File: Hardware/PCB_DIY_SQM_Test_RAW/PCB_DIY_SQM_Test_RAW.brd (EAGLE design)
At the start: 53 x 59.7 mm, 10 parts, among them U1 MLX90614_, U2 ARDUINO_SHIELDLONGPADS

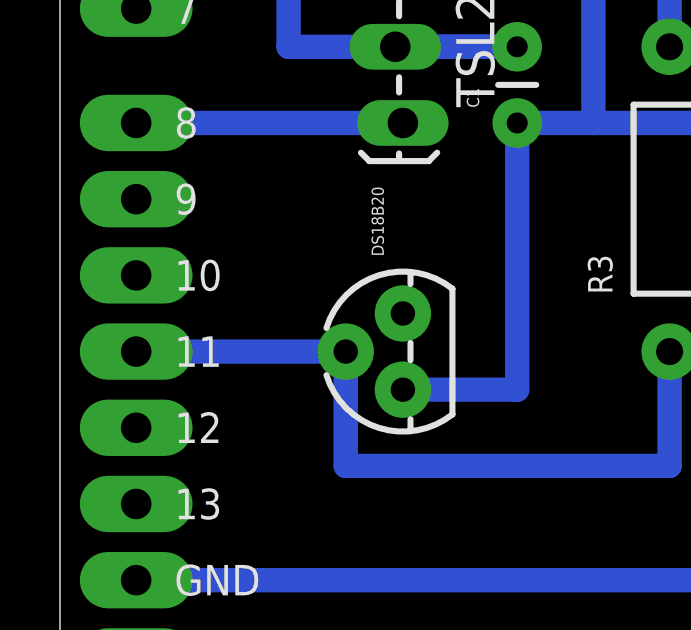
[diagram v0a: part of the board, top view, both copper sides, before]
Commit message: The DS18B20 now connects to Arduino pin #10 instead of pin #11. This allows us to use the Wireless SD shield (which uses pin #11 for SPI)
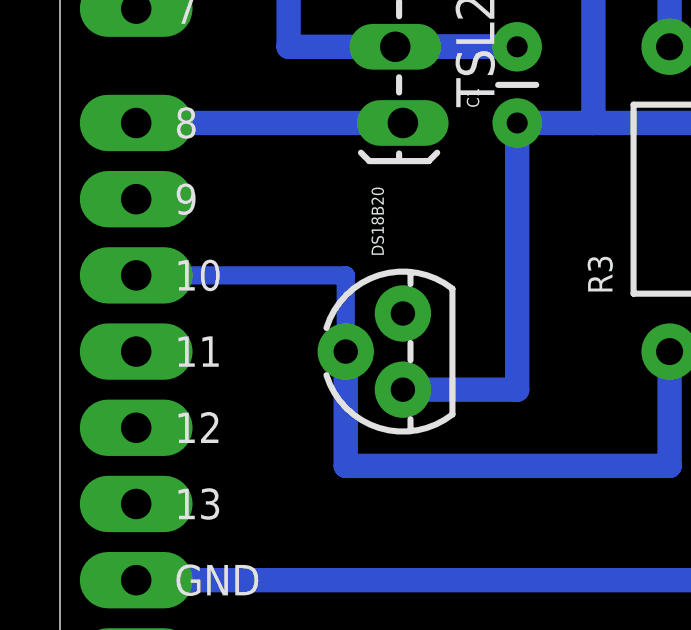
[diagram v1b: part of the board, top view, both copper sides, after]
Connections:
- net DS18B20P2: now also U2.D10; no longer U2.D11
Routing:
- net DS18B20P2: track 25.4 -> 27.9 mm
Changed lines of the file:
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@@
 <signal name="DS18B20P2">
 <contactref element="DS18B20" pad="2"/>
-<contactref element="U2" pad="D11"/>
 <contactref element="R3" pad="P$1"/>
 <wire x1="20.32" y1="25.4" x2="20.32" y2="21.59" width="0.8128" layer="16"/>
 <wire x1="20.32" y1="21.59" x2="9.525" y2="21.59" width="0.8128" layer="16"/>
 <wire x1="9.525" y1="21.59" x2="9.525" y2="25.4" width="0.8128" layer="16"/>
-<wire x1="9.525" y1="25.4" x2="2.54" y2="25.4" width="0.8128" layer="16"/>
+<contactref element="U2" pad="D10"/>
+<wire x1="2.54" y1="27.94" x2="9.525" y2="27.94" width="0.6096" layer="16"/>
+<wire x1="9.525" y1="27.94" x2="9.525" y2="25.4" width="0.6096" layer="16"/>
 </signal>
 <signal name="5V">

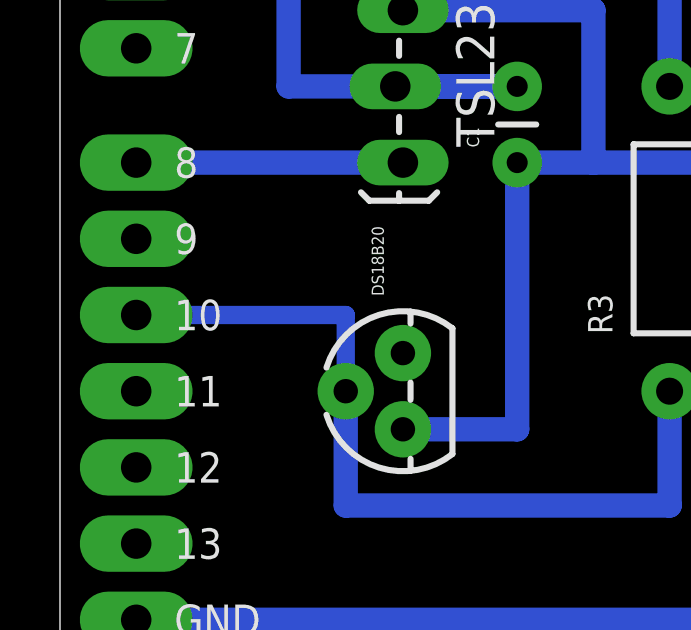
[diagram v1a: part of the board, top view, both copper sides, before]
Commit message: DS18B20 now uses Arduino pin #9 instead of #10, because #10 is used by the SD card of the wireless SD shield. Added support for SD cards. The sketch writes the data to a file called test.txt on the sd card (if available)
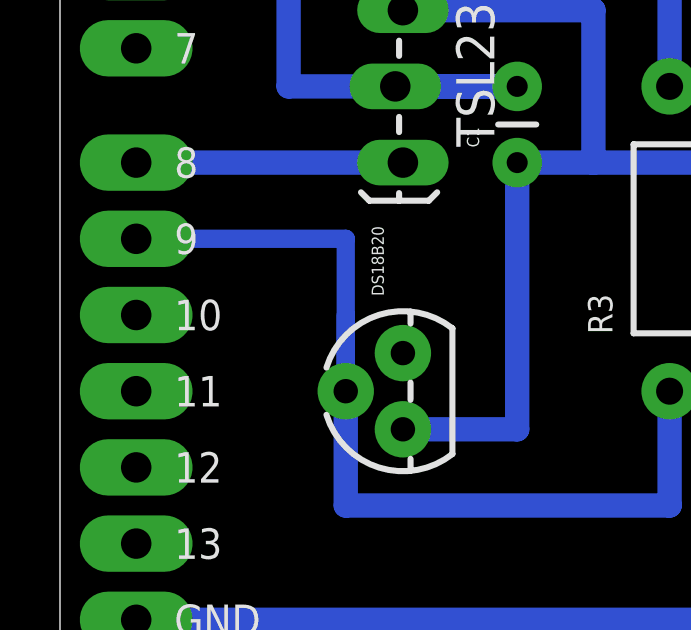
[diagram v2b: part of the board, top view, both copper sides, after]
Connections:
- net DS18B20P2: now also U2.D9; no longer U2.D10
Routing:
- net DS18B20P2: track 27.9 -> 33.0 mm
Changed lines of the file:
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@@
 <wire x1="20.32" y1="21.59" x2="9.525" y2="21.59" width="0.8128" layer="16"/>
 <wire x1="9.525" y1="21.59" x2="9.525" y2="25.4" width="0.8128" layer="16"/>
-<contactref element="U2" pad="D10"/>
-<wire x1="2.54" y1="27.94" x2="9.525" y2="27.94" width="0.6096" layer="16"/>
 <wire x1="9.525" y1="27.94" x2="9.525" y2="25.4" width="0.6096" layer="16"/>
+<contactref element="U2" pad="D9"/>
+<wire x1="2.54" y1="30.48" x2="9.525" y2="30.48" width="0.6096" layer="16"/>
+<wire x1="9.525" y1="30.48" x2="9.525" y2="25.4" width="0.6096" layer="16"/>
 </signal>
 <signal name="5V">

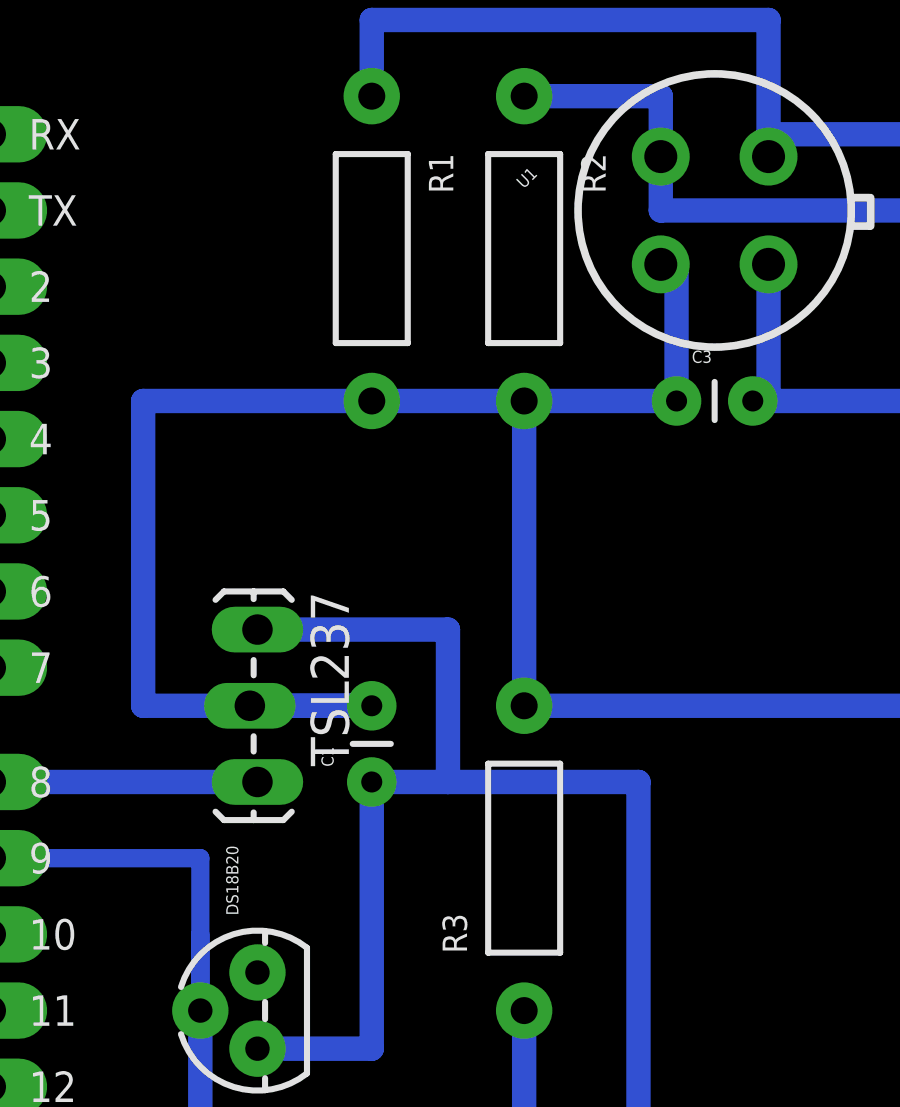
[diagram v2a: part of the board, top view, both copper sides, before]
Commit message: all resitsors are 4.7 kilo ohms.
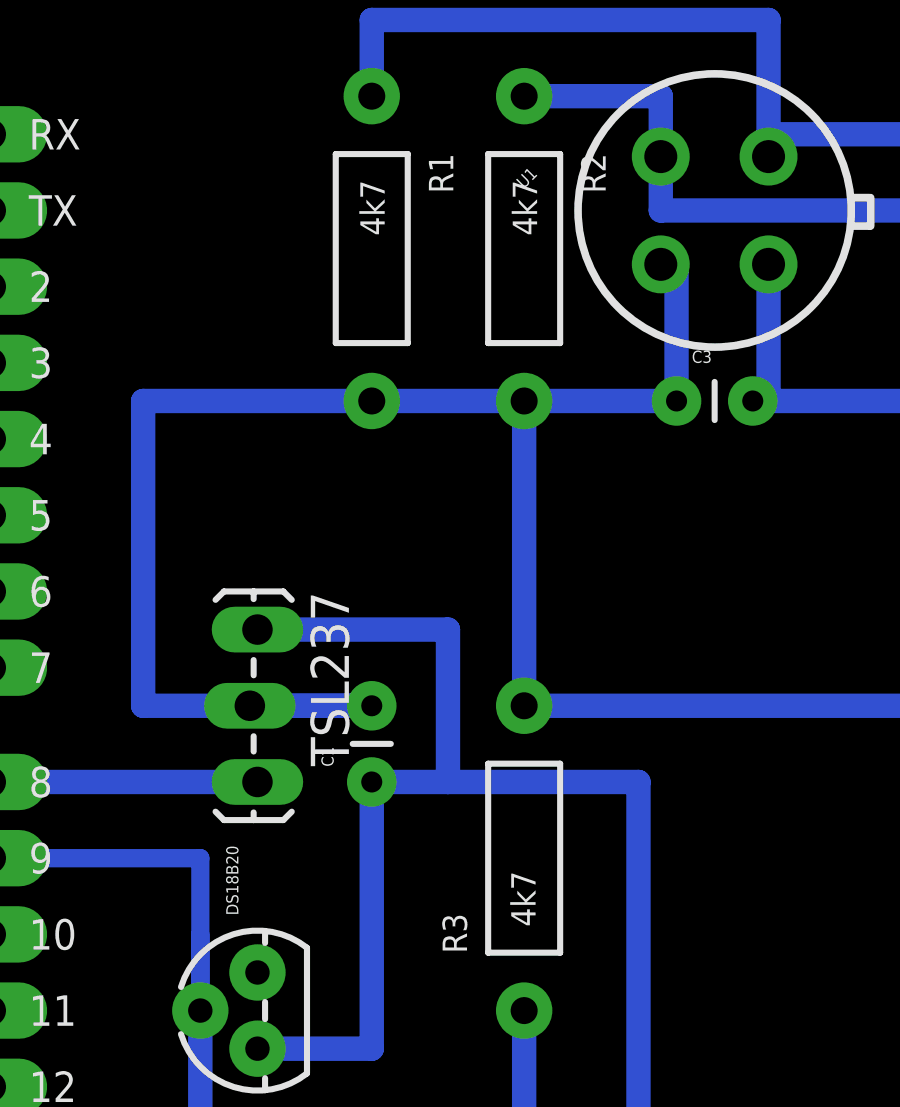
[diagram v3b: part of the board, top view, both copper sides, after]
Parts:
- R1, R2, R3: value (none) -> 4k7
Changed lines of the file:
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@@
 <element name="DS18B20" library="SparkFun-Sensors" package="TO-92" value="TEMPERATURE-SENSOR" x="11.43" y="25.4" rot="R90"/>
 <element name="TSL237" library="SparkFun-Connectors" package="1X03_LOCK_LONGPADS" value="" x="11.43" y="38.1" rot="R270"/>
-<element name="R1" library="SparkFun-Passives" package="AXIAL-0.4" value="" x="15.24" y="50.8" rot="R270"/>
-<element name="R2" library="SparkFun-Passives" package="AXIAL-0.4" value="" x="20.32" y="50.8" rot="R270"/>
-<element name="R3" library="SparkFun-Passives" package="AXIAL-0.4" value="" x="20.32" y="30.48" rot="R90"/>
+<element name="R1" library="SparkFun-Passives" package="AXIAL-0.4" value="4k7" x="15.24" y="50.8" rot="R270"/>
+<element name="R2" library="SparkFun-Passives" package="AXIAL-0.4" value="4k7" x="20.32" y="50.8" rot="R270"/>
+<element name="R3" library="SparkFun-Passives" package="AXIAL-0.4" value="4k7" x="20.32" y="30.48" rot="R90"/>
 <element name="C1" library="SparkFun-Passives" package="CAP-PTH-SMALL" value="100nF" x="15.24" y="33.02" rot="R90"/>
 <element name="C3" library="SparkFun-Passives" package="CAP-PTH-SMALL" value="100nF" x="25.4" y="45.72"/>
